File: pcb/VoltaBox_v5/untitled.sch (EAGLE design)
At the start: 55 parts, among them J1 1050170001, Q1 32768Hz, Q3 8MHz, X1 112J-TDAR-R(MICROSD)

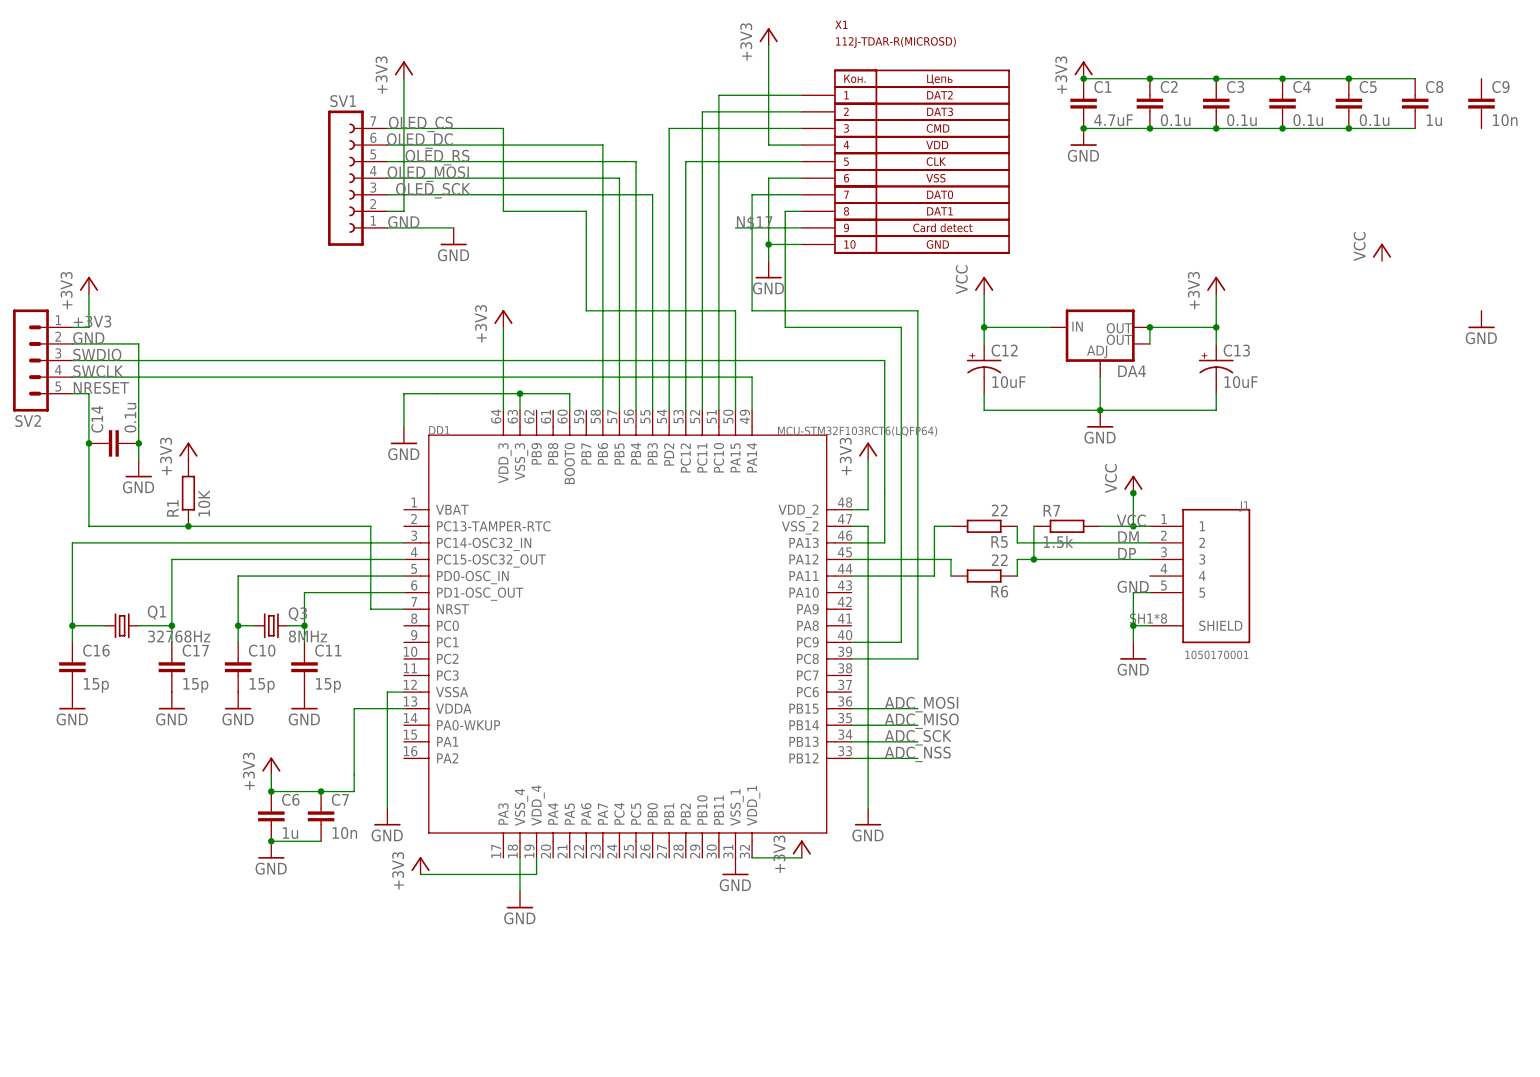
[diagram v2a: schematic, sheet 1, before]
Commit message: micro usb to usb-b, dc-dc inductor replaced, some schematic changes
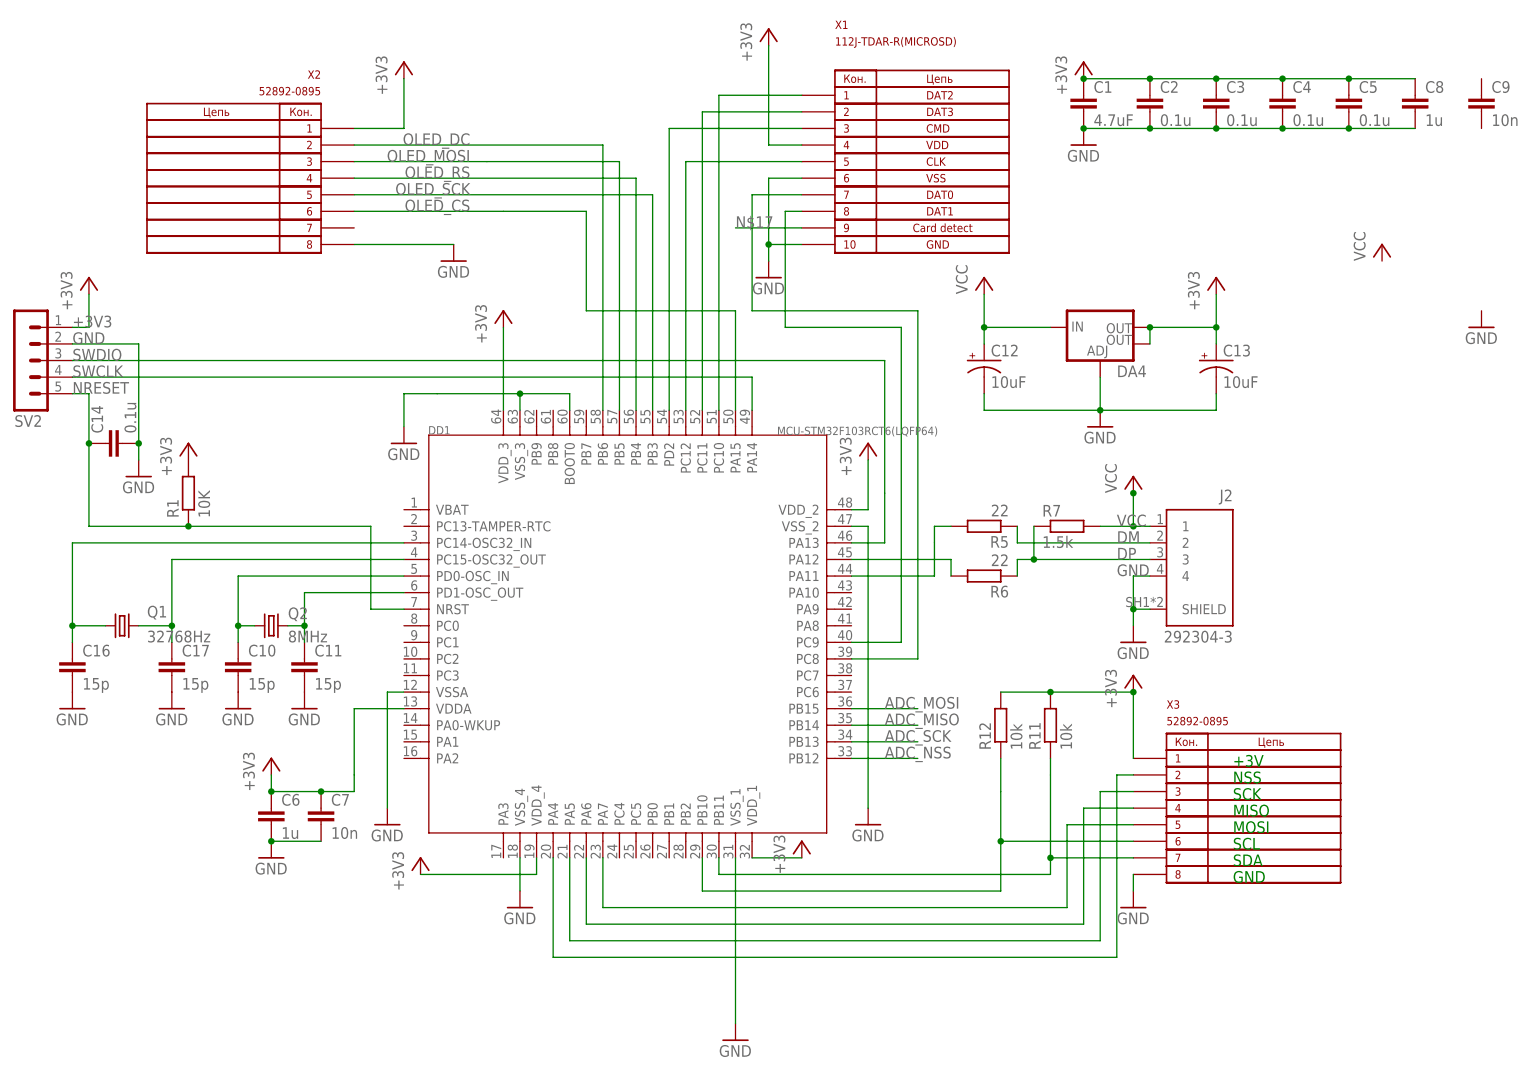
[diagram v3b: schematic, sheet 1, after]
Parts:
- removed J1: 1050170001, 1050170001:1050170001
- removed SV1: (no value), con-lsta:FE07-1
- added C32: 10uF, SparkFun-Capacitors:10UF-POLAR-EIA3216-16V-10%(TANT)
- added J2: 292304-3, 292304-3:292304-3
- added R11, R12: 10k, resistor:R-EU_R0603
- added X2, X3: 52892-0895, 52892-0895:52892-0895
- L1: value 8.5u -> B82477G4; device untitled:DR1030 -> untitled:B82477G4
- renumbered Q3 to Q2
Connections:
- new net GND1: X2.P$8
- new net N$24: DD1.PB11, R11.1, X3.P$7
- new net N$27: DD1.PB10, R12.1, X3.P$6
- new net N$28: DD1.PA7, X3.P$5
- new net N$29: DD1.PA6, X3.P$4
- new net N$30: DD1.PA5, X3.P$3
- new net N$31: DD1.PA4, X3.P$2
- net +3V3: now also R11.2, R12.2, X2.P$1, X3.P$1; no longer SV1.2
- net +5V: now also C32.+
- net DM: now also J2.2; no longer J1.2
- net DP: now also J2.3; no longer J1.3
- net GND: now also C32.-, J2.4, J2.SHIELD, X3.P$8; no longer J1.5, J1.SHIELD, SV1.1
- net OLED_CS: now also X2.P$6; no longer SV1.7
- net OLED_DC: now also X2.P$2; no longer SV1.6
- net OLED_MOSI: now also X2.P$3; no longer SV1.4
- net OLED_RS: now also X2.P$4; no longer SV1.5
- net OLED_SCK: now also X2.P$5; no longer SV1.3
- net VCC: now also J2.1; no longer J1.1
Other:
- note added: "+3V"
- note added: "GND"
- note added: "MISO"
- note added: "MOSI"
- note added: "NSS"
- note added: "SCK"
- note added: "SCL"
- note added: "SDA"

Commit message: Some pcb changes, dc-dc capacitors replaced.
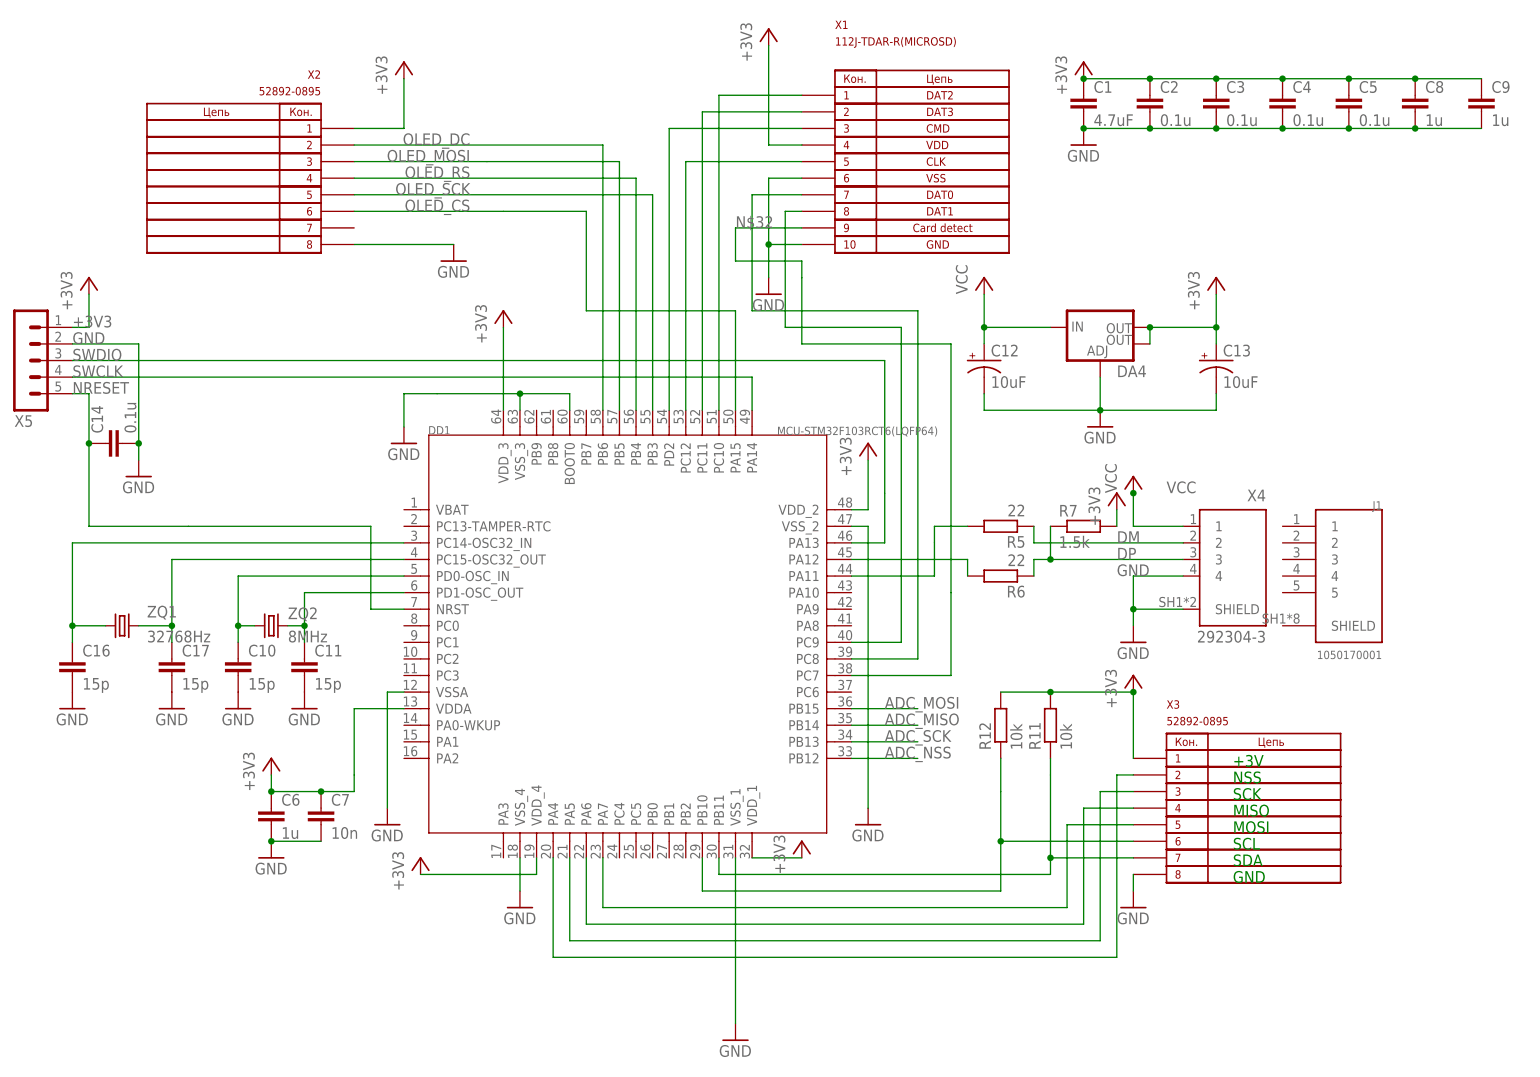
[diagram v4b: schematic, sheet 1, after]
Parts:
- removed C24: 10uF, SparkFun-Capacitors:10UF-1210-50V-20%
- removed J2: 292304-3, 292304-3:292304-3
- removed R1: 10K, resistor:R-EU_R0603
- added J1: 1050170001, 1050170001:1050170001
- added X4: 292304-3, 292304-3:292304-3
- C21: value 100uF -> 100u; device SparkFun-Capacitors:100UF-POLAR-EIA7343-10V-10%(TANT) -> rcl:CPOL-US150CLZ-1014
- C23: value 10uF -> 4.7u; device SparkFun-Capacitors:10UF-1210-50V-20% -> rcl:C-EUC2220K
- C25: device eagle-ltspice:CC0603 -> eagle-ltspice:CC1206
- C9: value 10n -> 1u
- R10: value 3.3K -> 2.7K
- R9: value 3.3K -> 1.2K
- renumbered Q1 to ZQ1, Q2 to ZQ2, SV2 to X5
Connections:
- removed net GND1: X2.P$8
- removed net N$17: X1.P$9
- new net N$32: DD1.PC7, X1.P$9
- net +12V: no longer C24.1
- net +3V3: now also C9.1, R7.2; no longer R1.2
- net DM: now also X4.2; no longer J2.2
- net DP: now also X4.3; no longer J2.3
- net GND: now also C9.2, X2.P$8, X4.4, X4.SHIELD; no longer C24.2, J2.4, J2.SHIELD
- net NRESET: no longer R1.1
- net VCC: now also X4.1; no longer J2.1, R7.2
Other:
- moved on the sheet: C23, R5, R6, R7
